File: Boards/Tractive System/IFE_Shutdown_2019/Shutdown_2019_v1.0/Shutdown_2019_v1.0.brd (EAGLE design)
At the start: 88.9 x 76.2 mm, 70 parts, among them Q11 DMP3099L-7, Q12 IRLML6346PBF, Q13 IRLML6346PBF, Q14 IRLML6346PBF, Q15 DMP3099L-7, Q16 DMN6140L-7, Q17 IRLML6346PBF, Q3 DMN6140L-7, Q4 DMN6140L-7, Q5 DMN6140L-7, Q6 DMP3099L-7, Q7 DMN6140L-7, Q8 DMN6140L-7, U1 STM32F103CBT6

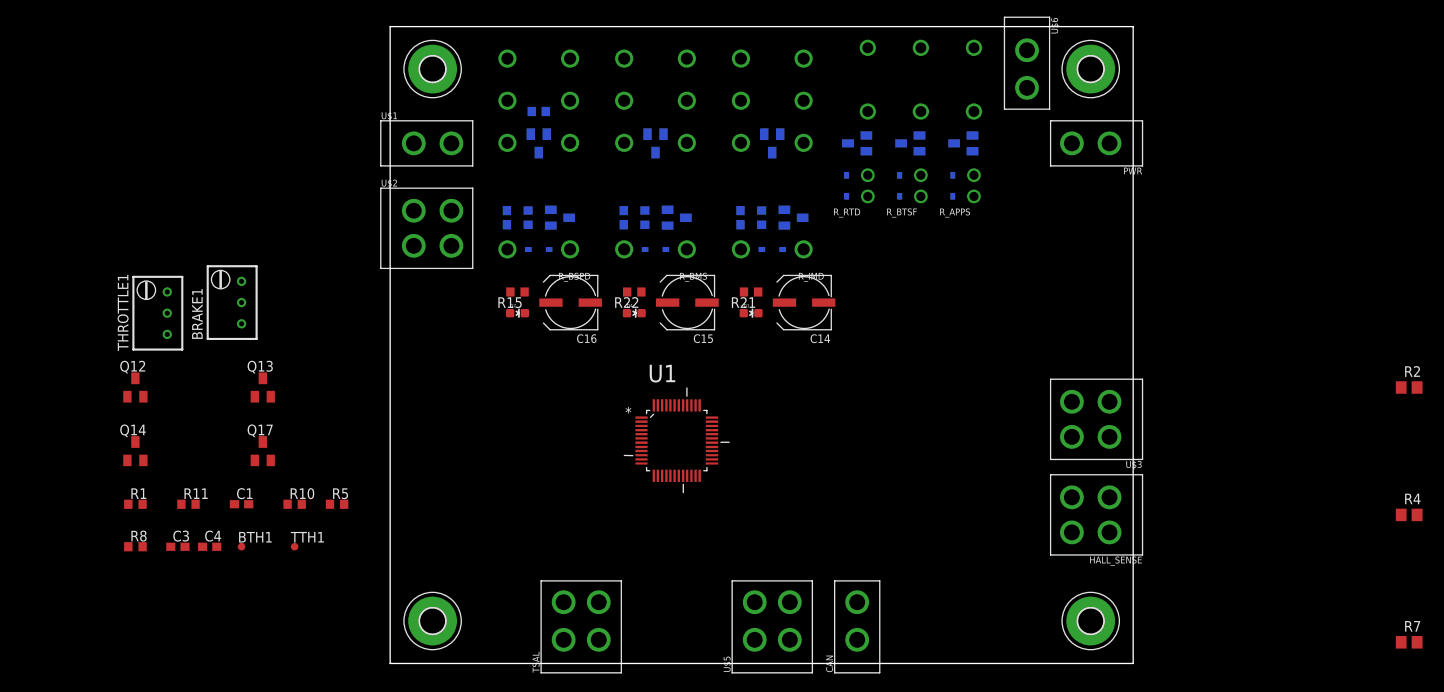
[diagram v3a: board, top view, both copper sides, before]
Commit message: Working on Power Supply and Light Drivers for Safety Board
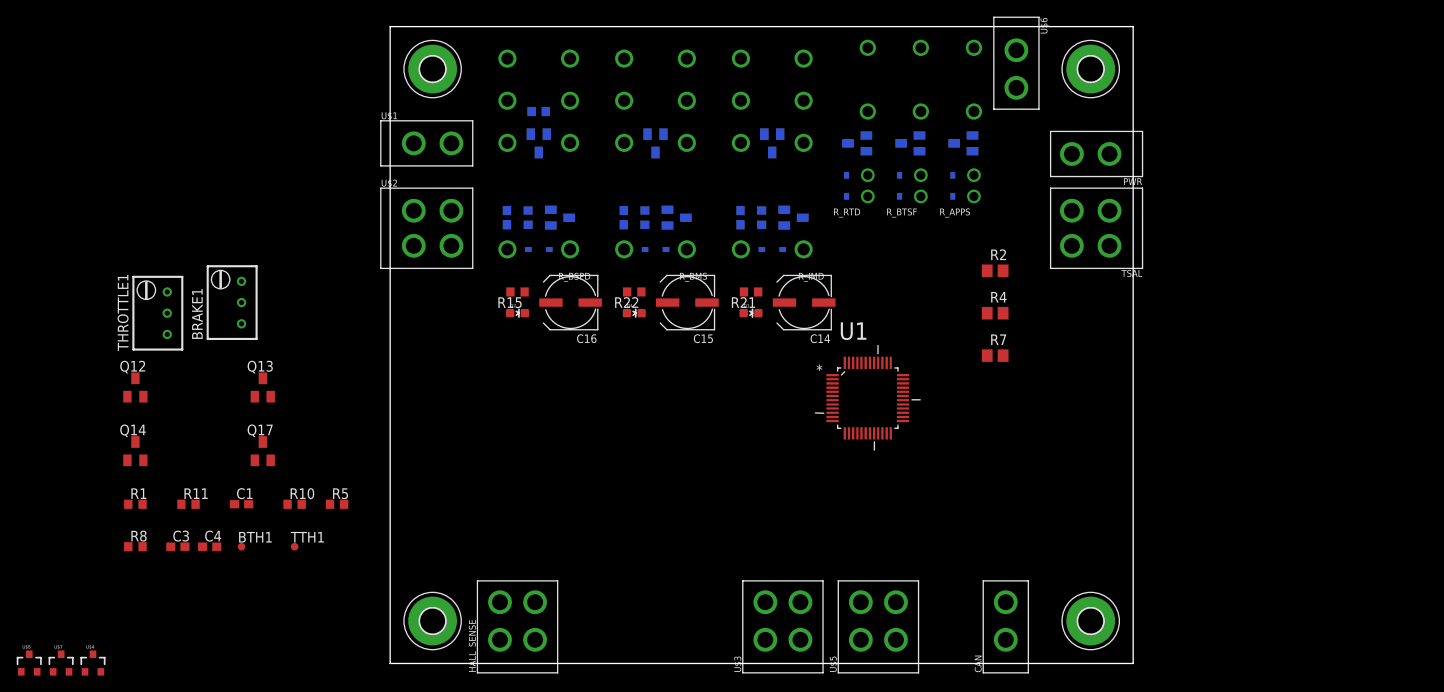
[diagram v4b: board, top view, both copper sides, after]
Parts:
- added U$4, U$7, U$8: DNBT8105, DIODES_INC:SOT23-3
- moved TSAL 77.0 mm to (83.8, 52.1), turned to 90 degrees
- moved HALL_SENSE 69.7 mm to (15.2, 5.08), turned to 0 degrees
- moved R7 60.2 mm to (72.4, 36.8)
- moved R4 55.1 mm to (72.4, 41.9)
- moved R2 51.5 mm to (72.4, 47.0)
- moved U$3 44.0 mm to (47.0, 5.08), turned to 0 degrees
- moved U1 23.4 mm to (57.1, 31.8)
- moved CAN 17.8 mm to (73.7, 5.08)
- moved U$5 12.7 mm to (58.4, 5.08)
- moved PWR 1.27 mm to (83.8, 61.0)
- moved U$6 1.27 mm to (74.9, 71.1)
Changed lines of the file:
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@@
 </autorouter>
 <elements>
-<element name="TSAL" library="Display_Custom" package="MINIFIT_JR_5566-04" value="MINIFIT_JR_5566-04" x="22.86" y="5.08"/>
-<element name="PWR" library="Display_Custom" package="MINIFIT_JR_5566-02" value="MINIFIT_JR_5566-02" x="83.82" y="62.23" rot="R90"/>
-<element name="CAN" library="Display_Custom" package="MINIFIT_JR_5566-02" value="MINIFIT_JR_5566-02" x="55.88" y="5.08"/>
+<element name="TSAL" library="Display_Custom" package="MINIFIT_JR_5566-04" value="MINIFIT_JR_5566-04" x="83.82" y="52.07" rot="R90"/>
+<element name="PWR" library="Display_Custom" package="MINIFIT_JR_5566-02" value="MINIFIT_JR_5566-02" x="83.82" y="60.96" rot="R90"/>
+<element name="CAN" library="Display_Custom" package="MINIFIT_JR_5566-02" value="MINIFIT_JR_5566-02" x="73.66" y="5.08"/>
 <element name="U$2" library="Display_Custom" package="MINIFIT_JR_5566-04" value="MINIFIT_JR_5566-04" x="5.08" y="52.07" rot="R270"/>
-<element name="U$3" library="Display_Custom" package="MINIFIT_JR_5566-04" value="MINIFIT_JR_5566-04" x="83.82" y="29.21" rot="R90"/>
-<element name="U$5" library="Display_Custom" package="MINIFIT_JR_5566-04" value="MINIFIT_JR_5566-04" x="45.72" y="5.08"/>
+<element name="U$3" library="Display_Custom" package="MINIFIT_JR_5566-04" value="MINIFIT_JR_5566-04" x="46.99" y="5.08"/>
+<element name="U$5" library="Display_Custom" package="MINIFIT_JR_5566-04" value="MINIFIT_JR_5566-04" x="58.42" y="5.08"/>
 <element name="U$1" library="Display_Custom" package="MINIFIT_JR_5566-02" value="MINIFIT_JR_5566-02" x="5.08" y="62.23" rot="R270"/>
-<element name="U$6" library="Display_Custom" package="MINIFIT_JR_5566-02" value="MINIFIT_JR_5566-02" x="76.2" y="71.12" rot="R180"/>
-<element name="HALL_SENSE" library="Display_Custom" package="MINIFIT_JR_5566-04" value="MINIFIT_JR_5566-04" x="83.82" y="17.78" rot="R90"/>
+<element name="U$6" library="Display_Custom" package="MINIFIT_JR_5566-02" value="MINIFIT_JR_5566-02" x="74.93" y="71.12" rot="R180"/>
+<element name="HALL_SENSE" library="Display_Custom" package="MINIFIT_JR_5566-04" value="MINIFIT_JR_5566-04" x="15.24" y="5.08"/>
 <element name="Q5" library="TRANS" package="SOT23" value="DMN6140L-7" x="20.32" y="53.34" rot="MR90"/>
 <element name="D2" library="Diodes" package="SOD323-F" value="1N914" x="17.78" y="49.53" rot="MR180"/>
@@
 <element name="H4" library="holes" library_urn="urn:adsk.eagle:library:237" package="3,0-PAD" package3d_urn="urn:adsk.eagle:package:14280/1" value="MOUNT-PAD-ROUND3.0" x="5.08" y="71.12"/>
 <element name="Q4" library="TRANS" package="SOT23" value="DMN6140L-7" x="68.58" y="62.23" rot="MR270"/>
-<element name="R2" library="Resistors" package="R0805" value="10k" x="121.92" y="33.02"/>
+<element name="R2" library="Resistors" package="R0805" value="10k" x="72.39" y="46.99"/>
 <element name="Q7" library="TRANS" package="SOT23" value="DMN6140L-7" x="62.23" y="62.23" rot="MR270"/>
-<element name="R4" library="Resistors" package="R0805" value="10k" x="121.92" y="17.78"/>
+<element name="R4" library="Resistors" package="R0805" value="10k" x="72.39" y="41.91"/>
 <element name="Q8" library="TRANS" package="SOT23" value="DMN6140L-7" x="55.88" y="62.23" rot="MR270"/>
-<element name="R7" library="Resistors" package="R0805" value="10k" x="121.92" y="2.54"/>
-<element name="U1" library="ST Microelctronics_By_element14_Batch_1" package="QFP50P900X900X160-48N" value="STM32F103CBT6" x="34.29" y="26.67">
-<attribute name="MPN" value="STM32F103CBT6" x="34.29" y="26.67" size="1.778" layer="27" display="off"/>
-<attribute name="OC_FARNELL" value="1606327" x="34.29" y="26.67" size="1.778" layer="27" display="off"/>
-<attribute name="OC_NEWARK" value="11N8296" x="34.29" y="26.67" size="1.778" layer="27" display="off"/>
-<attribute name="PACKAGE" value="QFP-48" x="34.29" y="26.67" size="1.778" layer="27" display="off"/>
-<attribute name="SUPPLIER" value="STMICROELECTRONICS" x="34.29" y="26.67" size="1.778" layer="27" display="off"/>
+<element name="R7" library="Resistors" package="R0805" value="10k" x="72.39" y="36.83"/>
+<element name="U1" library="ST Microelctronics_By_element14_Batch_1" package="QFP50P900X900X160-48N" value="STM32F103CBT6" x="57.15" y="31.75">
+<attribute name="MPN" value="STM32F103CBT6" x="57.15" y="31.75" size="1.778" layer="27" display="off"/>
+<attribute name="OC_FARNELL" value="1606327" x="57.15" y="31.75" size="1.778" layer="27" display="off"/>
+<attribute name="OC_NEWARK" value="11N8296" x="57.15" y="31.75" size="1.778" layer="27" display="off"/>
+<attribute name="PACKAGE" value="QFP-48" x="57.15" y="31.75" size="1.778" layer="27" display="off"/>
+<attribute name="SUPPLIER" value="STMICROELECTRONICS" x="57.15" y="31.75" size="1.778" layer="27" display="off"/>
 </element>
 <element name="R15" library="resistor" library_urn="urn:adsk.eagle:library:348" package="R0603" package3d_urn="urn:adsk.eagle:package:26057/1" value="900" x="15.24" y="44.45" rot="R180"/>
@@
 <element name="Q14" library="TRANS" package="SOT23" value="IRLML6346PBF" x="-30.48" y="25.4"/>
 <element name="Q17" library="TRANS" package="SOT23" value="IRLML6346PBF" x="-15.24" y="25.4"/>
+<element name="U$4" library="DIODES_INC" package="SOT23-3" value="DNBT8105" x="-35.56" y="0"/>
+<element name="U$7" library="DIODES_INC" package="SOT23-3" value="DNBT8105" x="-39.37" y="0"/>
+<element name="U$8" library="DIODES_INC" package="SOT23-3" value="DNBT8105" x="-43.18" y="0"/>
 </elements>
 <signals>
@@
 <contactref element="Q14" pad="2"/>
 <contactref element="Q17" pad="2"/>
-<wire x1="86.07" y1="62.23" x2="83.82" y2="71.12" width="0" layer="19" extent="1-1"/>
-<wire x1="69.68" y1="61.28" x2="86.07" y2="62.23" width="0" layer="19" extent="16-16"/>
+<wire x1="86.07" y1="60.96" x2="83.82" y2="71.12" width="0" layer="19" extent="1-1"/>
+<wire x1="69.68" y1="61.28" x2="86.07" y2="60.96" width="0" layer="19" extent="16-16"/>
 <wire x1="63.33" y1="61.28" x2="69.68" y2="61.28" width="0" layer="19" extent="16-16"/>
 <wire x1="56.98" y1="61.28" x2="63.33" y2="61.28" width="0" layer="19" extent="16-16"/>
@@
 <wire x1="-26.67" y1="44.45" x2="-17.78" y2="45.72" width="0" layer="19" extent="1-1"/>
 <wire x1="5.08" y1="5.08" x2="-16.93" y2="19.05" width="0" layer="19" extent="1-1"/>
-<wire x1="120.97" y1="33.02" x2="86.07" y2="62.23" width="0" layer="19" extent="1-1"/>
-<wire x1="120.97" y1="17.78" x2="120.97" y2="33.02" width="0" layer="19" extent="1-1"/>
-<wire x1="120.97" y1="2.54" x2="120.97" y2="17.78" width="0" layer="19" extent="1-1"/>
-<wire x1="83.82" y1="5.08" x2="120.97" y2="2.54" width="0" layer="19" extent="1-1"/>
+<wire x1="71.44" y1="46.99" x2="86.07" y2="60.96" width="0" layer="19" extent="1-1"/>
+<wire x1="71.44" y1="41.91" x2="71.44" y2="46.99" width="0" layer="19" extent="1-1"/>
+<wire x1="71.44" y1="36.83" x2="71.44" y2="41.91" width="0" layer="19" extent="1-1"/>
+<wire x1="83.82" y1="5.08" x2="71.44" y2="36.83" width="0" layer="19" extent="1-1"/>
 </signal>
 <signal name="TSAL_LV-">
@@
 <contactref element="U$6" pad="1"/>
 <contactref element="R_APPS" pad="4"/>
-<wire x1="69.85" y1="73.66" x2="76.2" y2="68.87" width="0" layer="19" extent="1-1"/>
+<wire x1="69.85" y1="73.66" x2="74.93" y2="68.87" width="0" layer="19" extent="1-1"/>
 </signal>
 <signal name="ENABLE_OUT">
 <contactref element="U$6" pad="2"/>
 <contactref element="R_RTD" pad="3"/>
-<wire x1="57.15" y1="66.04" x2="76.2" y2="73.37" width="0" layer="19" extent="1-1"/>
+<wire x1="57.15" y1="66.04" x2="74.93" y2="73.37" width="0" layer="19" extent="1-1"/>
 </signal>
 <signal name="HALL_RL">
@@
 <contactref element="Q4" pad="1"/>
 <contactref element="R2" pad="2"/>
-<wire x1="69.68" y1="63.18" x2="122.87" y2="33.02" width="0" layer="19" extent="1-16"/>
+<wire x1="69.68" y1="63.18" x2="73.34" y2="46.99" width="0" layer="19" extent="1-16"/>
 </signal>
 <signal name="BTSF_EN">
 <contactref element="Q7" pad="1"/>
 <contactref element="R4" pad="2"/>
-<wire x1="63.33" y1="63.18" x2="122.87" y2="17.78" width="0" layer="19" extent="1-16"/>
+<wire x1="63.33" y1="63.18" x2="73.34" y2="41.91" width="0" layer="19" extent="1-16"/>
 </signal>
 <signal name="RTD_EN">
 <contactref element="Q8" pad="1"/>
 <contactref element="R7" pad="2"/>
-<wire x1="56.98" y1="63.18" x2="122.87" y2="2.54" width="0" layer="19" extent="1-16"/>
+<wire x1="56.98" y1="63.18" x2="73.34" y2="36.83" width="0" layer="19" extent="1-16"/>
 </signal>
 <signal name="N$12">

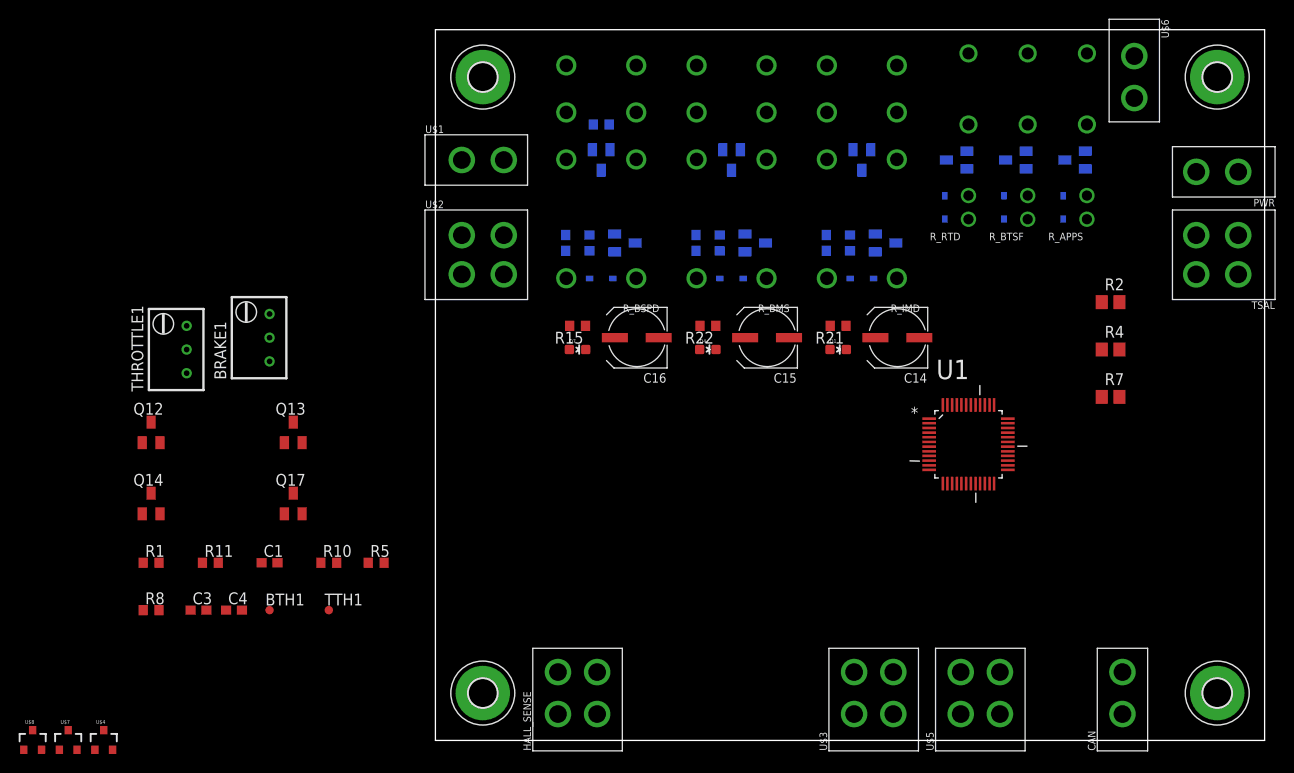
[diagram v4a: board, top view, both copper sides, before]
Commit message: Finishing power distribution on safety board
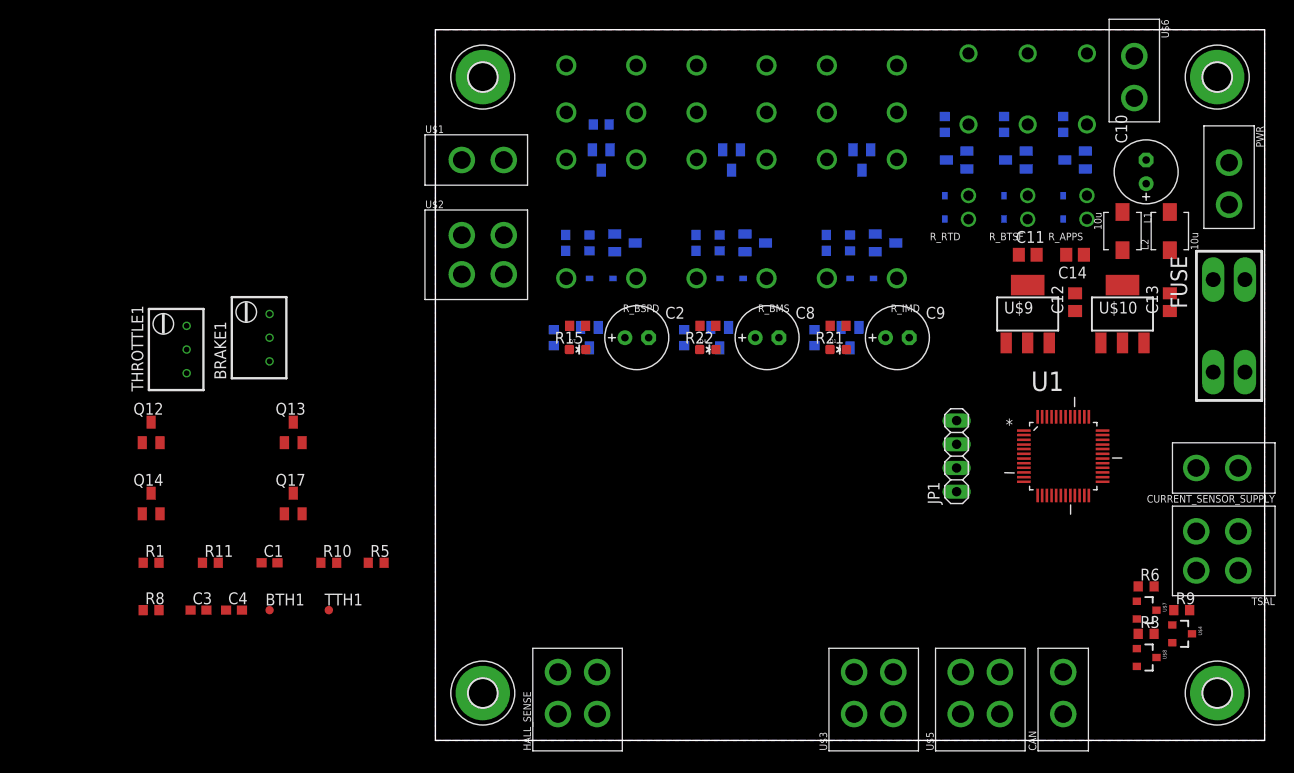
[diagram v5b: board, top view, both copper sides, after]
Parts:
- removed C15, C16: 47uF, rcl:UD-6,3X5,8_NICHICON
- added C10: 220u, rcl:E2,5-7
- added C11: 2.2u, rcl:C0805
- added C12, C13: 4.7u, rcl:C0805
- added C2, C8, C9: 47u, rcl:E2,5-7
- added CURRENT_SENSOR_SUPPLY: MINIFIT_JR_5566-02, Display_Custom:MINIFIT_JR_5566-02
- added FUSE: MINI297-3568, Fuse:3568
- added JP1: (no value), Headers_IFE:1X04
- added L1, L2: 10u, SparkFun-Passives:INDUCTOR-SRP4020
- added Q1, Q2, Q9: DMN6140L-7, TRANS:SOT23
- added R12, R13, R14: 10k, resistor:R0603
- added R3, R6: 3.6k, rcl:R0603
- added R9: (no value), rcl:R0603
- added U$10: SPX1117M3-L-5-0, MAXLINEAR:SOT223
- added U$9: SPX1117M3-L-3-3, MAXLINEAR:SOT223
- C14: value 47uF -> 2.2u; device rcl:UD-6,3X5,8_NICHICON -> rcl:C0805
- R2, R4, R7: device Resistors:R0805 -> rcl:R0603
- moved U$8 119.7 mm to (76.2, 8.89), turned to 270 degrees
- moved U$7 116.4 mm to (76.2, 14.0), turned to 270 degrees
- moved U$4 116.1 mm to (80.0, 11.4), turned to 270 degrees
- moved R7 34.2 mm to (54.6, 66.0), flipped to the bottom, turned to 270 degrees
- moved TSAL 31.8 mm to (83.8, 20.3)
- moved R4 26.7 mm to (61.0, 66.0), flipped to the bottom, turned to 270 degrees
- moved C14 21.0 mm to (68.6, 52.1)
- moved R2 19.7 mm to (67.3, 66.0), flipped to the bottom, turned to 270 degrees
- moved U1 10.2 mm to (67.3, 30.5)
- moved CAN 6.35 mm to (67.3, 5.08)
- moved PWR 1.80 mm to (85.1, 59.7), turned to 180 degrees
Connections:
- removed net BMS1_FAULT_INDICATOR: C15.+, D9.C, R22.1, R_BMS.21, R_BMS.A1
- removed net BSPD_FAULT_INDICATOR: C16.+, D2.C, R15.1, R_BSPD.21, R_BSPD.A1
- removed net BSPD_FAULT_INDICATOR1: D3.C
- removed net BSPD_FAULT_INDICATOR2: D5.C
- removed net BSPD_FAULT_INDICATOR3: D6.C
- removed net IMD_FAULT_INDICATOR: C14.+, D15.C, R21.1, R_IMD.21, R_IMD.A1
- new net +3V3: C11.1, R12.2, R13.2, R14.2, U$9.2, U$9.4
- new net BRAKE_LIGHT_EN: R9.1
- new net FAULT_BMS_STAT: C8.+, D9.C, R22.1, R_BMS.21, R_BMS.A1
- new net FAULT_BMS_STATUS: Q2.1
- new net FAULT_BMS_STATUS_3_3: Q2.3, R13.1
- new net FAULT_BSPD_STAT: C2.+, D2.C, R15.1, R_BSPD.21, R_BSPD.A1
- new net FAULT_BSPD_STATUS: Q1.1
- new net FAULT_BSPD_STATUS_3_3: Q1.3, R12.1
- new net FAULT_IMD_STAT: C9.+, D15.C, R21.1, R_IMD.21, R_IMD.A1
- new net FAULT_IMD_STATUS: Q9.1
- new net FAULT_IMD_STATUS_3_3: Q9.3, R14.1
- new net N$15: R3.2, U$8.1
- new net N$16: R6.2, U$7.1
- new net N$3: R9.2, U$4.1
- new net N$5: C10.+, L1.P$1, L2.P$2
- new net N$6: FUSE.P$2, FUSE.P$3, L2.P$1
- new net TSAL_HV_EN: R3.1
- new net TSAL_LV_EN: R6.1
- net +12V: now also C12.1, C13.1, D3.C, D5.C, D6.C, L1.P$2, R_APPS.1, R_BTSF.1, R_RTD.1, U$10.3, U$9.3
- net +5V: now also C14.1, CURRENT_SENSOR_SUPPLY.1, U$10.2, U$10.4
- net BRAKE_LIGHT-: now also U$4.3
- net GND: now also C10.-, C11.2, C12.2, C13.2, C14.2, C2.-, C8.-, C9.-, CURRENT_SENSOR_SUPPLY.2, Q1.2, Q2.2, Q9.2, U$10.1, U$4.2, U$7.2, U$8.2, U$9.1; no longer C14.-, C15.-, C16.-
- net PWR: now also FUSE.P$1, FUSE.P$4
- net TSAL_HV-: now also U$8.3
- net TSAL_LV-: now also U$7.3
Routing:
- added copper zone on layer 1, net GND
- added copper zone on layer 16, net GND
